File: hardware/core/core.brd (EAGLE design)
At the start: 159.7 x 163.8 mm, 527 parts, among them IC1 MAX481CSA, IC10 MAX481CSA, IC11 MAX481CSA, IC12 MAX481CSA, IC13 MAX481CSA, IC14 MAX481CSA, IC15 MAX481CSA, IC16 MAX481CSA, IC17 MAX481CSA, IC18 MAX481CSA, IC19 MAX481CSA, IC2 LD117AS12TR, IC20 MAX481CSA, IC21 MAX481CSA, IC22 LD117AS12TR, IC23 LD117AS12TR, IC3 MAX481CSA, IC4 MAX481CSA, IC5 MAX481CSA, IC6 MAX481CSA, IC7 MAX481CSA, IC8 MAX481CSA, IC9 MAX481CSA

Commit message: Progress
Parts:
- added JP3, JP4: (no value), pinhead:2X02
- moved R27 51.6 mm to (74.9, 11.4)
- moved R26 48.2 mm to (67.3, 11.4)
- moved D84 19.5 mm to (62.2, 48.9)
- moved R129 19.5 mm to (58.4, 48.9)
- moved D83 10.3 mm to (71.1, 43.8)
- moved R127 10.3 mm to (67.3, 43.8)
- moved D81 10.3 mm to (71.1, 48.9)
- moved R125 10.3 mm to (67.3, 48.9)
- moved D85 1.42 mm to (80.0, 43.8)
- moved R128 1.42 mm to (76.2, 43.8)
- moved D82 1.42 mm to (80.0, 48.9)
- moved R126 1.42 mm to (76.2, 48.9)
- moved C2 1.27 mm to (99.1, 22.9)
- moved C35 1.27 mm to (109.2, 22.9)
- moved C36 1.27 mm to (109.2, 12.7)
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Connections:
- net 33: now also NEBULA_H.19
- net 35: no longer NEBULA_H.19
- net GND: now also JP3.1, JP3.2, JP3.3, JP3.4, JP4.1, JP4.2, JP4.3, JP4.4
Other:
- board text added: "3v 5v 12v Enable"
- board text removed: "3v 5v 12v eStop"

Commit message: Update boards to remove interrupt for all but expansion H
Update boards to remove interrupt for all but expansion H
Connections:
- net 18: no longer NEBULA_E.19
- net 19: no longer NEBULA_F.19
- net 33: no longer NEBULA_G.19, NEBULA_H.19
- net 34: no longer NEBULA_A.19
- net 35: no longer NEBULA_B.19
- net 36: no longer NEBULA_C.19
- net 39: now also NEBULA_H.19; no longer NEBULA_D.19
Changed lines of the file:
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@@
 <signal name="36">
 <contactref element="U$1" pad="17"/>
-<contactref element="NEBULA_C" pad="19"/>
-<wire x1="74.92" y1="28.375" x2="81.915" y2="86.52" width="0" layer="19" extent="1-1"/>
 </signal>
 <signal name="39">
 <contactref element="U$1" pad="18"/>
-<contactref element="NEBULA_D" pad="19"/>
-<wire x1="72.38" y1="28.375" x2="51.435" y2="86.52" width="0" layer="19" extent="1-1"/>
+<contactref element="NEBULA_H" pad="19"/>
+<wire x1="72.38" y1="28.375" x2="36.83" y2="72.55" width="0" layer="19" extent="1-1"/>
 </signal>
 <signal name="34">
 <contactref element="U$1" pad="19"/>
-<contactref element="NEBULA_A" pad="19"/>
-<wire x1="69.84" y1="28.375" x2="143.51" y2="86.52" width="0" layer="19" extent="1-1"/>
 </signal>
 <signal name="35">
 <contactref element="U$1" pad="20"/>
-<contactref element="NEBULA_B" pad="19"/>
-<wire x1="67.3" y1="28.375" x2="112.395" y2="86.52" width="0" layer="19" extent="1-1"/>
 </signal>
 <signal name="32">
@@
 <signal name="33">
 <contactref element="U$1" pad="22"/>
-<contactref element="NEBULA_G" pad="19"/>
-<contactref element="NEBULA_H" pad="19"/>
-<wire x1="36.83" y1="72.55" x2="67.945" y2="72.55" width="0" layer="19" extent="1-1"/>
-<wire x1="62.22" y1="28.375" x2="67.945" y2="72.55" width="0" layer="19" extent="1-1"/>
 </signal>
 <signal name="25">
@@
 <signal name="19">
 <contactref element="U$1" pad="10"/>
-<contactref element="NEBULA_F" pad="19"/>
-<wire x1="64.76" y1="3.605" x2="128.905" y2="72.55" width="0" layer="19" extent="1-1"/>
 </signal>
 <signal name="18">
 <contactref element="U$1" pad="9"/>
-<contactref element="NEBULA_E" pad="19"/>
-<wire x1="62.22" y1="3.605" x2="20.32" y2="86.52" width="0" layer="19" extent="1-1"/>
 </signal>
 <signal name="5">

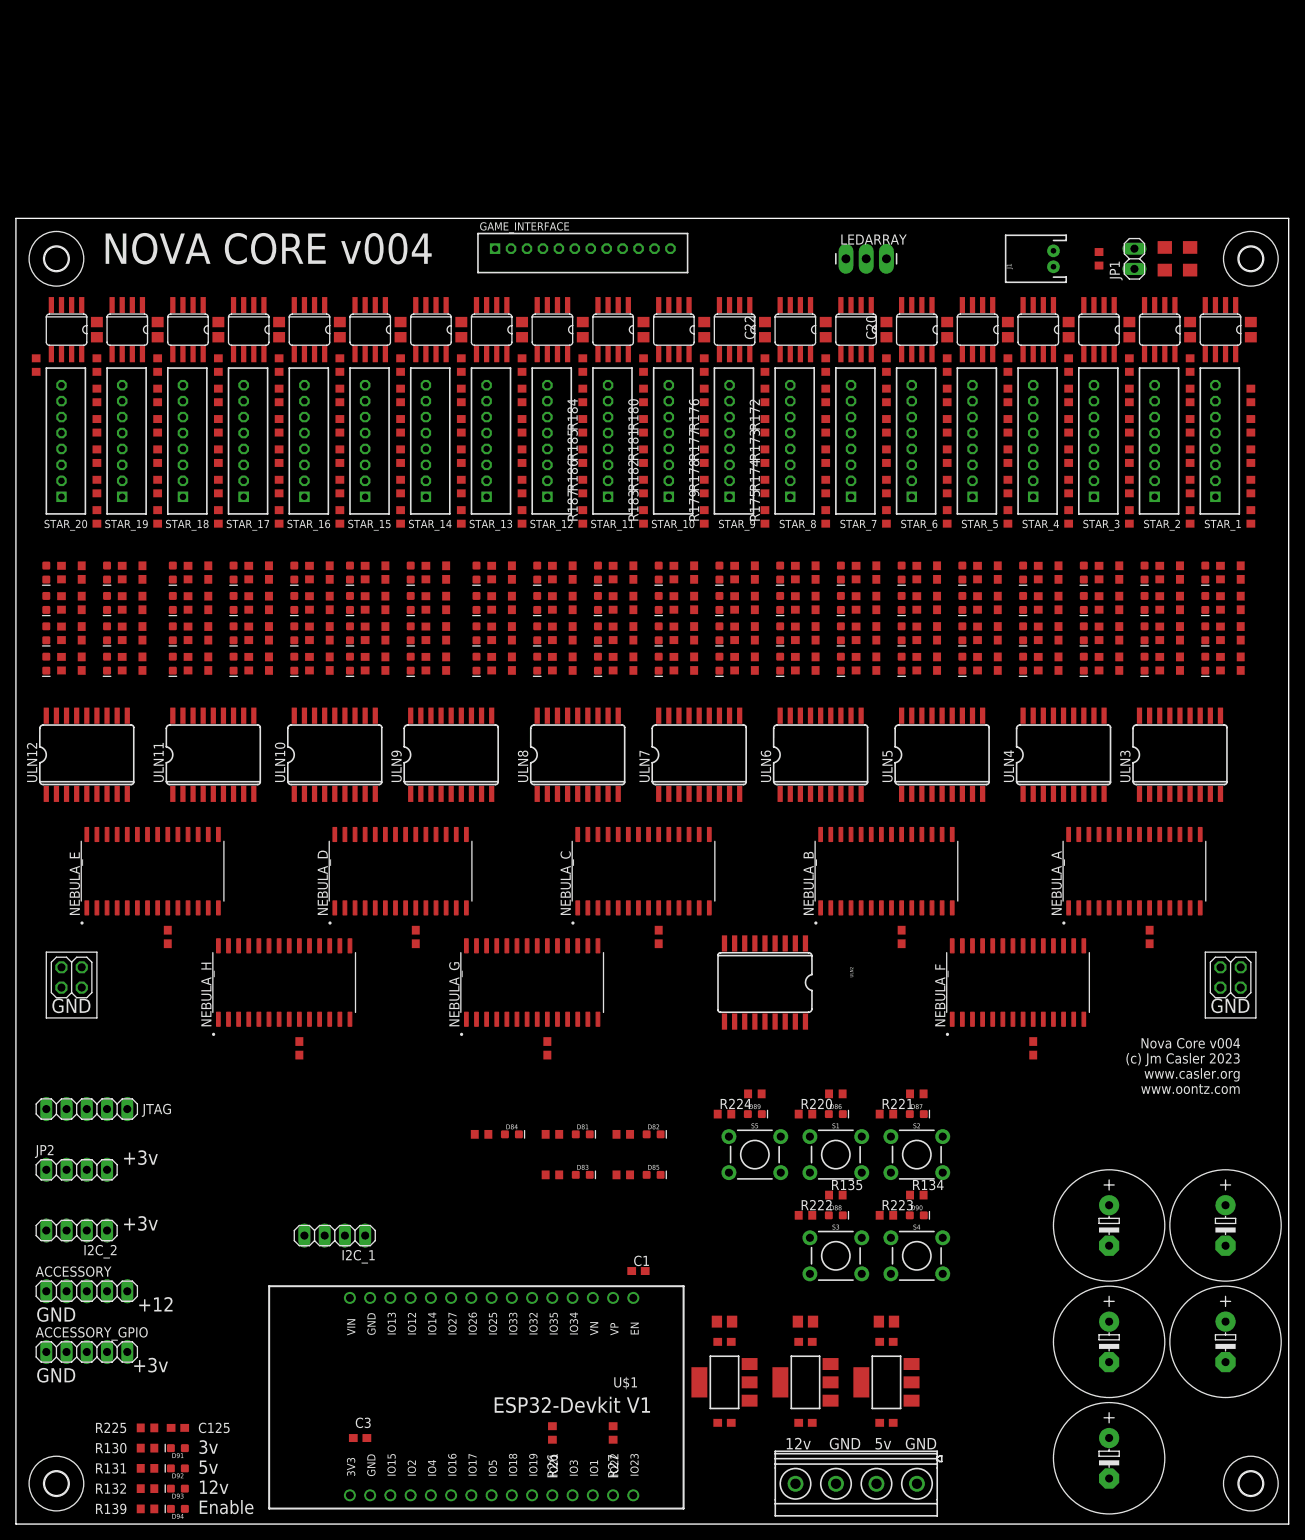
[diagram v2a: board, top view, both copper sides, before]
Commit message: Update phoenix connectors & add JLC_ROTATION
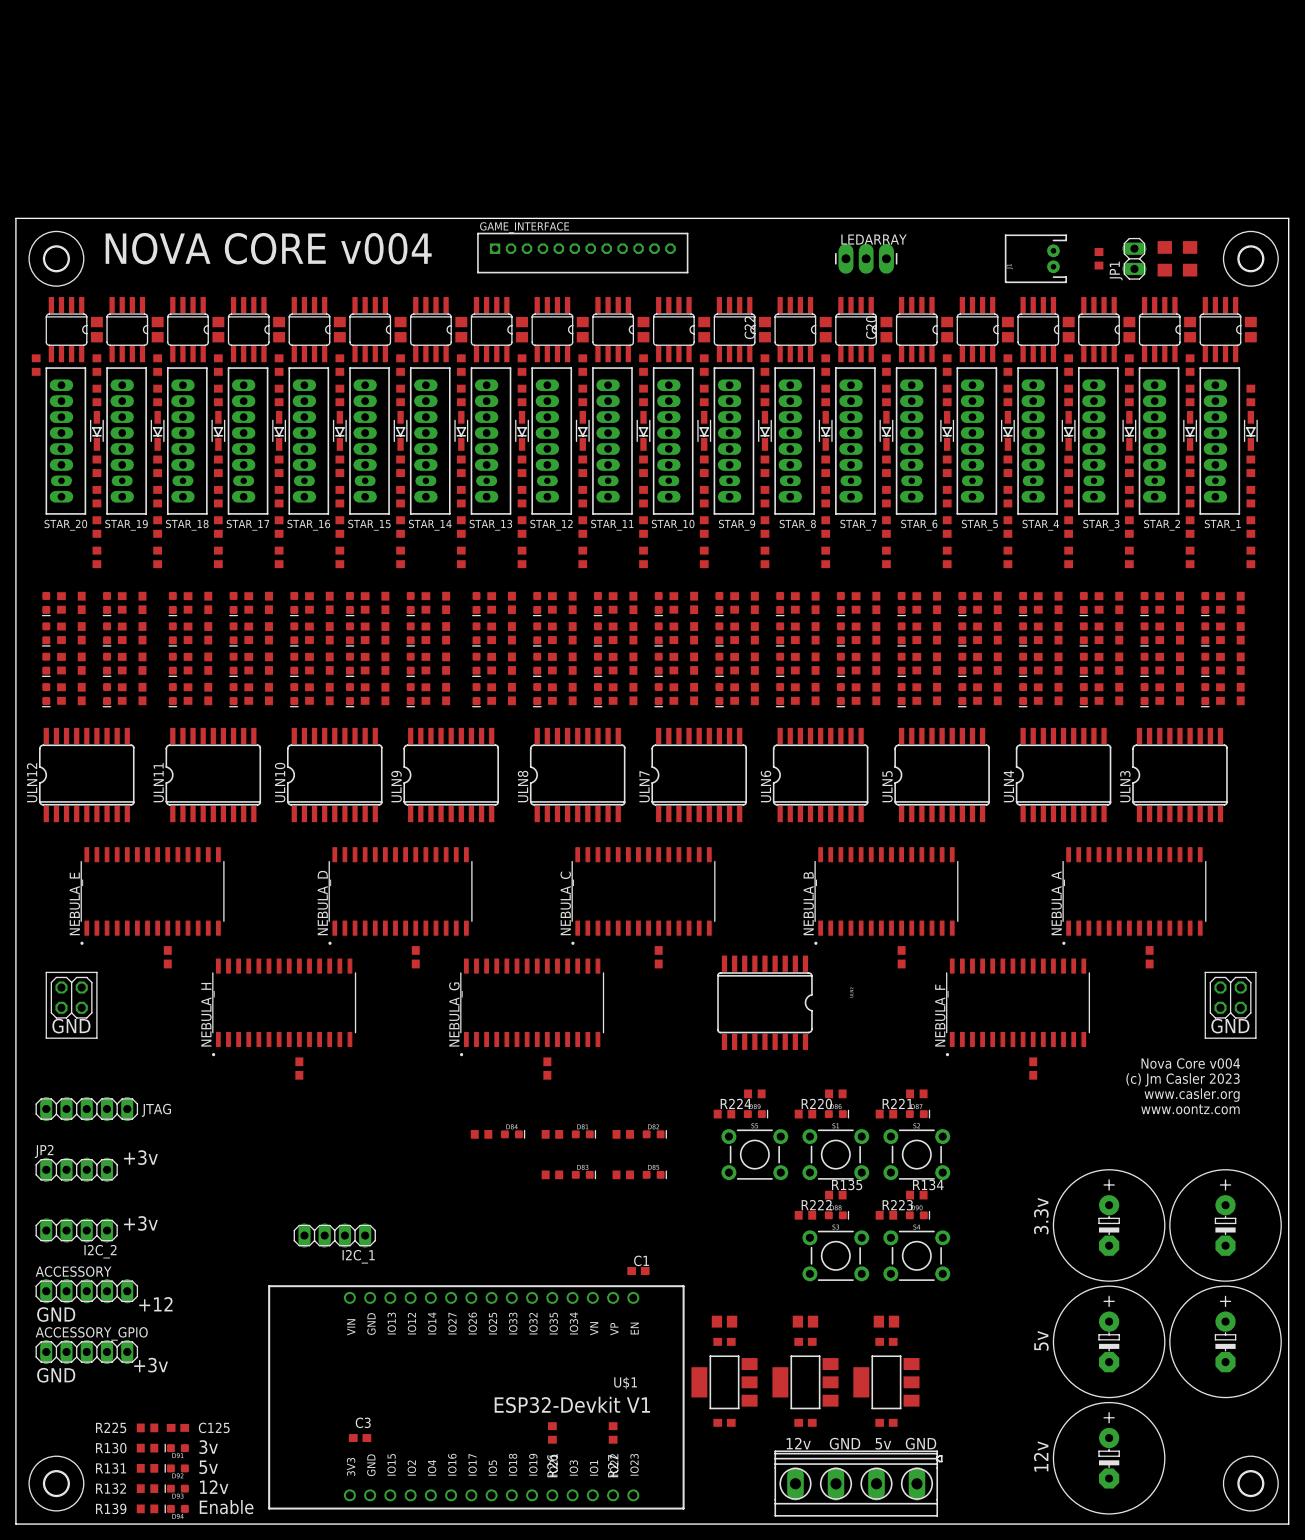
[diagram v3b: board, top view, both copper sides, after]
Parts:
- added D100, D101, D102, D103, D104, D105, D106, D107, D108, D109, D110, D111, D112, D113, D114, D95, D96, D97, D98, D99: D_B5819W-SL_CHANGJ_SOD123, JLC PCB Basic Parts_loc:SOD123
- POWER_IN: device con-phoenix-508:MKDSN1,5/4-5,08 -> con-phoenix-508-jm:MKDSN1,5/4-5,08
- R132: value R_1.8K_0603 -> R_1K_0603
- moved R141 5.08 mm to (154.9, 128.9)
- moved R142 5.08 mm to (154.9, 125.1)
- moved R145 5.08 mm to (147.3, 128.9)
- moved R146 5.08 mm to (147.3, 125.1)
- moved R149 5.08 mm to (139.7, 128.9)
- moved R150 5.08 mm to (139.7, 125.1)
- moved R153 5.08 mm to (132.1, 128.9)
- moved R154 5.08 mm to (132.1, 125.1)
- moved R157 5.08 mm to (124.5, 128.9)
- moved R158 5.08 mm to (124.5, 125.1)
- moved R161 5.08 mm to (116.8, 128.9)
- moved R162 5.08 mm to (116.8, 125.1)
- moved R165 5.08 mm to (109.2, 128.9)
- moved R166 5.08 mm to (109.2, 125.1)
- moved R169 5.08 mm to (101.6, 128.9)
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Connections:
- new net N$325: D95.C, STAR_1.6
- new net N$326: D97.C, STAR_3.6
- new net N$327: D96.A, R55.2
- new net N$328: D96.C, STAR_2.6
- new net N$329: D100.A, R59.2
- new net N$330: D100.C, STAR_6.6
- new net N$331: D99.A, R58.2
- new net N$332: D99.C, STAR_5.6
- new net N$333: D110.A, R85.2
- new net N$334: D110.C, STAR_15.6
- new net N$335: D109.A, R84.2
- new net N$336: D109.C, STAR_14.6
- new net N$337: D105.A, R103.2
- new net N$338: D105.C, STAR_17.6
- new net N$339: D112.A, R104.2
- new net N$340: D112.C, STAR_18.6
- new net N$341: D113.A, R105.2
- new net N$342: D113.C, STAR_19.6
- new net N$343: D114.A, R106.2
- new net N$344: D114.C, STAR_20.6
- net N$10: now also D102.A, R61.2; no longer R58.2, STAR_5.6
- net N$104: now also D108.A, R65.2; no longer R104.2, STAR_18.6
- net N$105: now also D108.C, STAR_12.6; no longer R105.2, STAR_19.6
- net N$106: now also D111.A, R86.2; no longer R106.2, STAR_20.6
- net N$107: now also D111.C, STAR_16.6; no longer R103.2, STAR_17.6
- net N$15: now also D102.C, STAR_8.6; no longer R59.2, STAR_6.6
- net N$16: now also D101.A; no longer STAR_7.6
- net N$17: now also D101.C, STAR_7.6; no longer R61.2, STAR_8.6
- net N$18: now also D103.A, R62.2; no longer R65.2, STAR_12.6
- net N$19: now also D103.C, STAR_9.6; no longer R64.2, STAR_11.6
- net N$2: now also D98.A, R57.2; no longer R55.2, STAR_2.6
- net N$24: now also D104.A, R83.2; no longer R63.2, STAR_10.6
- net N$25: now also D104.C, STAR_13.6; no longer R62.2, STAR_9.6
- net N$7: now also D98.C, STAR_4.6; no longer R56.2, STAR_3.6
- net N$72: now also D106.A, R63.2; no longer R84.2, STAR_14.6
- net N$73: now also D106.C, STAR_10.6; no longer R85.2, STAR_15.6
- net N$74: now also D107.A, R64.2; no longer R86.2, STAR_16.6
- net N$75: now also D107.C, STAR_11.6; no longer R83.2, STAR_13.6
- net N$8: now also D97.A, R56.2; no longer R57.2, STAR_4.6
- net N$9: now also D95.A; no longer STAR_1.6
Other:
- board text added: "12v"
- board text added: "3.3v"
- board text added: "5v"
